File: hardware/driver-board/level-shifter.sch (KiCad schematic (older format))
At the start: 3 parts, among them U1 TXS0108E

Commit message: Rework power to four different voltage domains
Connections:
- net +3V3 renamed +3V0
- net +5V renamed VCC
- net CLK_3V3 renamed CLK_3V
- net CS1_3V3 renamed CS1_3V
- net CS2_3V3 renamed CS2_3V
- net DC_3V3 renamed DC_3V
- net MISO_3V3 renamed MISO_3V
- net MOSI_3V3 renamed MOSI_3V
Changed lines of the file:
@@
-$EndComp
-$Comp
-L power:+3.3V #PWR01
-U 1 1 5EFF6A56
-P 5700 3800
-F 0 "#PWR01" H 5700 3650 50  0001 C CNN
-F 1 "+3.3V" V 5700 3900 50  0000 L CNN
-F 2 "" H 5700 3800 50  0001 C CNN
-F 3 "" H 5700 3800 50  0001 C CNN
-	1    5700 3800
-	0    -1   -1   0
-$EndComp
-$Comp
-L power:+3.3V #PWR03
-U 1 1 5EFF90BA
-P 5700 4600
-F 0 "#PWR03" H 5700 4450 50  0001 C CNN
-F 1 "+3.3V" V 5700 4700 50  0000 L CNN
-F 2 "" H 5700 4600 50  0001 C CNN
-F 3 "" H 5700 4600 50  0001 C CNN
-	1    5700 4600
-	0    -1   -1   0
 $EndComp
 $Comp
@@
 CS2
 Text GLabel 5450 4500 0    50   Output ~ 0
-CLK_3V3
+CLK_3V
 Text GLabel 5450 4400 0    50   Input ~ 0
-MISO_3V3
+MISO_3V
 Text GLabel 5450 4300 0    50   Output ~ 0
-MOSI_3V3
+MOSI_3V
 Text GLabel 5450 4200 0    50   Output ~ 0
-CS1_3V3
+CS1_3V
 Text GLabel 5450 4100 0    50   Output ~ 0
-CS2_3V3
+CS2_3V
 Text GLabel 5450 4000 0    50   Output ~ 0
-DC_3V3
+DC_3V
 $Comp
 L power:GND #PWR08
@@
 F 3 "" H 6450 5450 50  0001 C CNN
 	1    6450 5450
-	1    0    0    -1
-$EndComp
-$Comp
-L power:+5V #PWR06
-U 1 1 5F01AF06
-P 6450 5150
-F 0 "#PWR06" H 6450 5000 50  0001 C CNN
-F 1 "+5V" H 6465 5323 50  0000 C CNN
-F 2 "" H 6450 5150 50  0001 C CNN
-F 3 "" H 6450 5150 50  0001 C CNN
-	1    6450 5150
-	1    0    0    -1
-$EndComp
-$Comp
-L power:+5V #PWR02
-U 1 1 5F01B63A
-P 6500 3800
-F 0 "#PWR02" H 6500 3650 50  0001 C CNN
-F 1 "+5V" V 6500 3900 50  0000 L CNN
-F 2 "" H 6500 3800 50  0001 C CNN
-F 3 "" H 6500 3800 50  0001 C CNN
-	1    6500 3800
-	0    1    1    0
-$EndComp
-$Comp
-L power:+3.3V #PWR05
-U 1 1 5F01FA3A
-P 5750 5150
-F 0 "#PWR05" H 5750 5000 50  0001 C CNN
-F 1 "+3.3V" H 5765 5323 50  0000 C CNN
-F 2 "" H 5750 5150 50  0001 C CNN
-F 3 "" H 5750 5150 50  0001 C CNN
-	1    5750 5150
 	1    0    0    -1
 $EndComp
@@
 	1    0    0    -1
 $EndComp
+$Comp
+L power:+3V0 #PWR01
+U 1 1 5F04354C
+P 5700 3800
+F 0 "#PWR01" H 5700 3650 50  0001 C CNN
+F 1 "+3V0" V 5700 3900 50  0000 L CNN
+F 2 "" H 5700 3800 50  0001 C CNN
+F 3 "" H 5700 3800 50  0001 C CNN
+	1    5700 3800
+	0    -1   -1   0
+$EndComp
+$Comp
+L power:+3V0 #PWR03
+U 1 1 5F04366B
+P 5700 4600
+F 0 "#PWR03" H 5700 4450 50  0001 C CNN
+F 1 "+3V0" V 5700 4700 50  0000 L CNN
+F 2 "" H 5700 4600 50  0001 C CNN
+F 3 "" H 5700 4600 50  0001 C CNN
+	1    5700 4600
+	0    -1   -1   0
+$EndComp
+$Comp
+L power:+3V0 #PWR05
+U 1 1 5F04412C
+P 5750 5150
+F 0 "#PWR05" H 5750 5000 50  0001 C CNN
+F 1 "+3V0" H 5765 5323 50  0000 C CNN
+F 2 "" H 5750 5150 50  0001 C CNN
+F 3 "" H 5750 5150 50  0001 C CNN
+	1    5750 5150
+	1    0    0    -1
+$EndComp
+$Comp
+L power:VCC #PWR02
+U 1 1 5F049AAE
+P 6500 3800
+F 0 "#PWR02" H 6500 3650 50  0001 C CNN
+F 1 "VCC" V 6500 3900 50  0000 L CNN
+F 2 "" H 6500 3800 50  0001 C CNN
+F 3 "" H 6500 3800 50  0001 C CNN
+	1    6500 3800
+	0    1    1    0
+$EndComp
+$Comp
+L power:VCC #PWR06
+U 1 1 5F049E76
+P 6450 5150
+F 0 "#PWR06" H 6450 5000 50  0001 C CNN
+F 1 "VCC" H 6465 5323 50  0000 C CNN
+F 2 "" H 6450 5150 50  0001 C CNN
+F 3 "" H 6450 5150 50  0001 C CNN
+	1    6450 5150
+	1    0    0    -1
+$EndComp

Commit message: Add display schematics
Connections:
- no-connect marks 0 -> 4
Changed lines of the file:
@@
 $Descr A4 11693 8268
 encoding utf-8
-Sheet 2 6
+Sheet 2 7
 Title "FT81x TFT040 Driver Board"
-Date "2020-07-03"
+Date "2020-07-05"
 Rev "2007D"
 Comp ""
@@
 Comment4 ""
 $EndDescr
-$Comp
-L driver-board:TXS0108E U1
-U 1 1 5EFFB6A5
-P 6100 4150
-F 0 "U1" H 6100 4915 50  0000 C CNN
-F 1 "TXS0108E" H 6100 4824 50  0000 C CNN
-F 2 "Package_SO:TSSOP-20_4.4x6.5mm_P0.65mm" H 6100 4150 50  0001 C CNN
-F 3 "" H 6100 4150 50  0001 C CNN
-F 4 "C17206" H 6100 4733 50  0000 C CNN "JLCPCB"
-	1    6100 4150
-	1    0    0    -1
-$EndComp
 Wire Wire Line
 	6500 4000 6750 4000
@@
 	1    0    0    -1
 $EndComp
+$Comp
+L driver-board:TXS0108E U1
+U 1 1 5EFFB6A5
+P 6100 4150
+F 0 "U1" H 6100 4915 50  0000 C CNN
+F 1 "TXS0108E" H 6100 4824 50  0000 C CNN
+F 2 "Package_SO:TSSOP-20_4.4x6.5mm_P0.65mm" H 6100 4150 50  0001 C CNN
+F 3 "" H 6100 4150 50  0001 C CNN
+F 4 "C17206" H 6100 4733 50  0000 C CNN "JLCPCB"
+	1    6100 4150
+	1    0    0    -1
+$EndComp
+NoConn ~ 6500 3700
+NoConn ~ 6500 3900
+NoConn ~ 5700 3900
+NoConn ~ 5700 3700
 $EndSCHEMATC

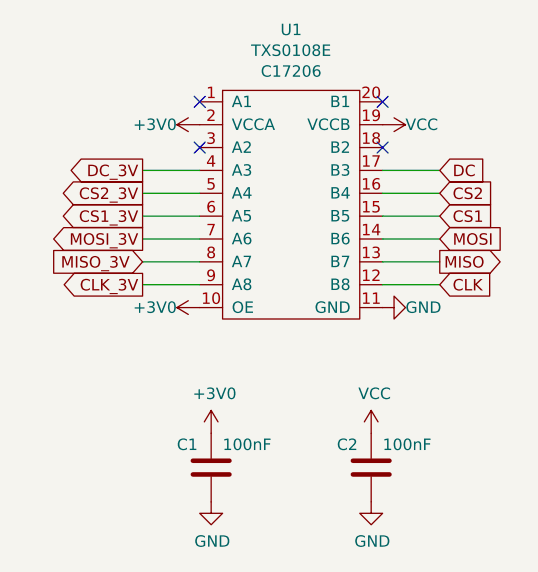
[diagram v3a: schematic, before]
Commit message: Adapt new SPI signal names from OSHWA
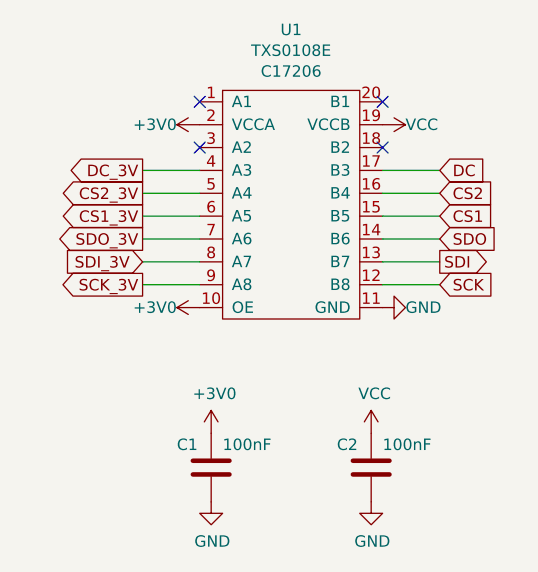
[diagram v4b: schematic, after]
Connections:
- net CLK renamed SCK
- net CLK_3V renamed SCK_3V
- net MISO renamed SDI
- net MISO_3V renamed SDI_3V
- net MOSI renamed SDO
- net MOSI_3V renamed SDO_3V
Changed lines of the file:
@@
 DC
 Text GLabel 6750 4500 2    50   Input ~ 0
-CLK
+SCK
 Text GLabel 6750 4400 2    50   Output ~ 0
-MISO
+SDI
 Text GLabel 6750 4300 2    50   Input ~ 0
-MOSI
+SDO
 Text GLabel 6750 4200 2    50   Input ~ 0
 CS1
@@
 CS2
 Text GLabel 5450 4500 0    50   Output ~ 0
-CLK_3V
+SCK_3V
 Text GLabel 5450 4400 0    50   Input ~ 0
-MISO_3V
+SDI_3V
 Text GLabel 5450 4300 0    50   Output ~ 0
-MOSI_3V
+SDO_3V
 Text GLabel 5450 4200 0    50   Output ~ 0
 CS1_3V

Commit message: Add missing JLCPCB part numbers
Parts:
- C1, C2: JLCPCB (none) -> C14663
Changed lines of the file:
@@
 F 2 "Capacitor_SMD:C_0603_1608Metric" H 5788 5150 50  0001 C CNN
 F 3 "~" H 5750 5300 50  0001 C CNN
+F 4 "C14663" H 5750 5300 50  0001 C CNN "JLCPCB"
 	1    5750 5300
 	1    0    0    -1
@@
 F 2 "Capacitor_SMD:C_0603_1608Metric" H 6488 5150 50  0001 C CNN
 F 3 "~" H 6450 5300 50  0001 C CNN
+F 4 "C14663" H 6450 5300 50  0001 C CNN "JLCPCB"
 	1    6450 5300
 	1    0    0    -1

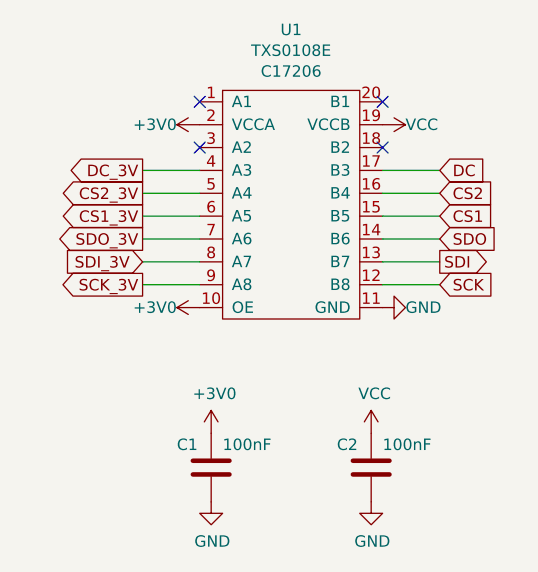
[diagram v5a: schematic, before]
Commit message: Rename JLCPCB to LCSC and update PCB
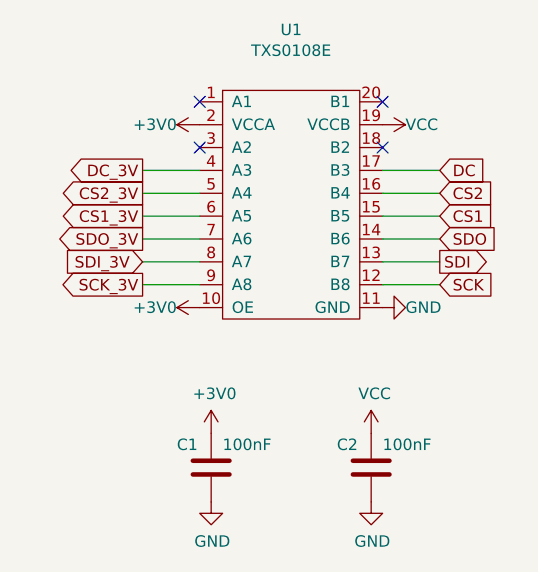
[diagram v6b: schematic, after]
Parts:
- C1, C2: JLCPCB C14663 -> (none); LCSC (none) -> C14663
- U1: JLCPCB C17206 -> (none); LCSC (none) -> C17206
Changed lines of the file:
@@
 F 2 "Capacitor_SMD:C_0603_1608Metric" H 5788 5150 50  0001 C CNN
 F 3 "~" H 5750 5300 50  0001 C CNN
-F 4 "C14663" H 5750 5300 50  0001 C CNN "JLCPCB"
+F 4 "C14663" H 5750 5300 50  0001 C CNN "LCSC"
 	1    5750 5300
 	1    0    0    -1
@@
 F 2 "Capacitor_SMD:C_0603_1608Metric" H 6488 5150 50  0001 C CNN
 F 3 "~" H 6450 5300 50  0001 C CNN
-F 4 "C14663" H 6450 5300 50  0001 C CNN "JLCPCB"
+F 4 "C14663" H 6450 5300 50  0001 C CNN "LCSC"
 	1    6450 5300
 	1    0    0    -1
@@
 F 2 "Package_SO:TSSOP-20_4.4x6.5mm_P0.65mm" H 6100 4150 50  0001 C CNN
 F 3 "" H 6100 4150 50  0001 C CNN
-F 4 "C17206" H 6100 4733 50  0000 C CNN "JLCPCB"
+F 4 "C17206" H 6100 4150 50  0001 C CNN "LCSC"
 	1    6100 4150
 	1    0    0    -1
